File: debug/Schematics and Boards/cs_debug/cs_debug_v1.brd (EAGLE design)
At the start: 38.1 x 44.5 mm, 239 parts, among them J1 J-JTAG-CORTEX_SMD, J19 Solar, J2 J-JTAG-CORTEX_SMD, J3 J-JTAG-CORTEX-NEEDLE6-LEGS, J4 J-SERIAL-PORT, J5 J-WURTH-USBC, Q10 2N7002P, Q3 FDN340P, Q4 2N7002P, Q5 FDN340P, Q6 2N7002P, Q7 FDN340P, Q8 2N7002P, Q9 FDN340P, U1 AP2120N-3.3TRG1, U10 OPA357AIDBVTG4, U11 DAC7574IDGS, U12 MCP73871T-2CCI/ML, U13 USB2412-DZK, U14 INA225AIDGK, U15 OPA357AIDBVTG4, U2 TLV1117LV33DCYR, U5 INA225AIDGK, U6 OPA357AIDBVTG4, U7 INA225AIDGK, U8 OPA357AIDBVTG4, U9 INA225AIDGK, Y1 EPSON_TSX-3225_24.0000MF10Z-C3, Y101 32.768kHz, Y102 12mHz-12pF-K7

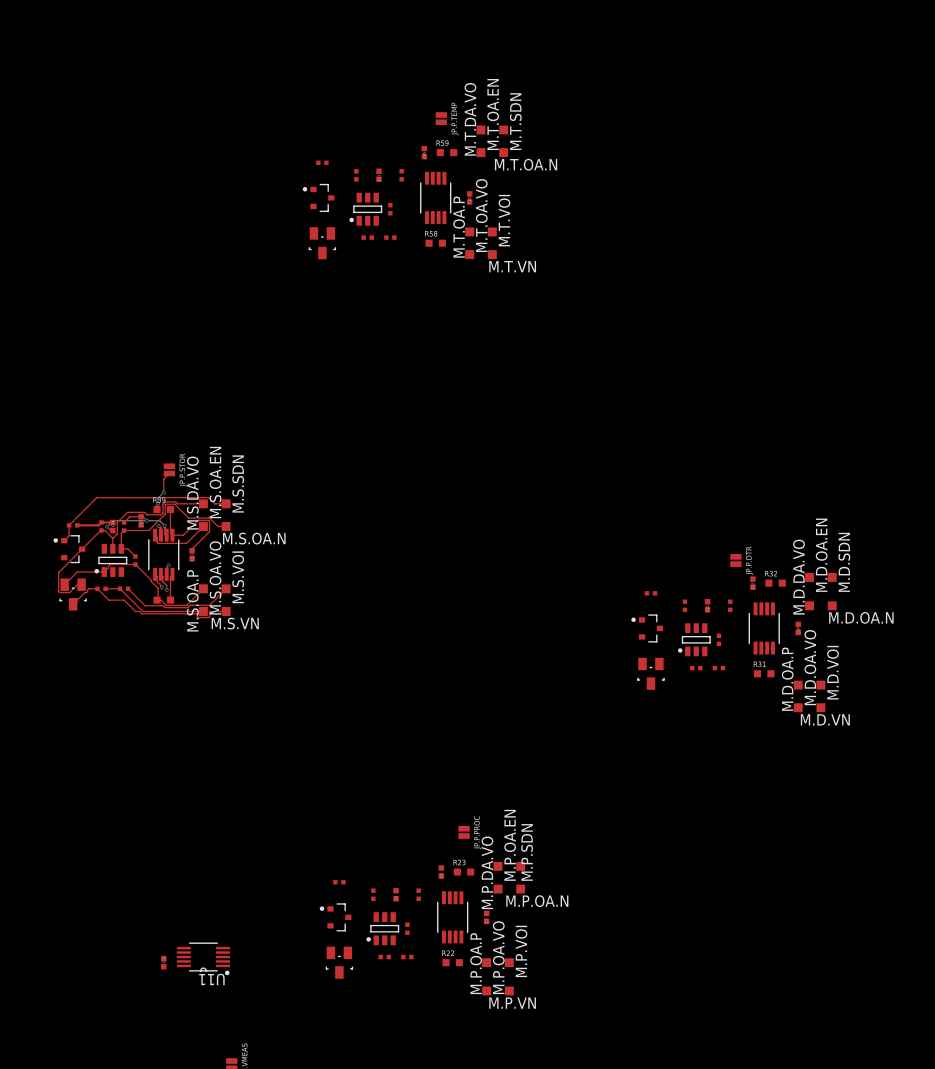
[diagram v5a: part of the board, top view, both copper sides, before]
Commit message: DBG- layout and hand-route for current monitors
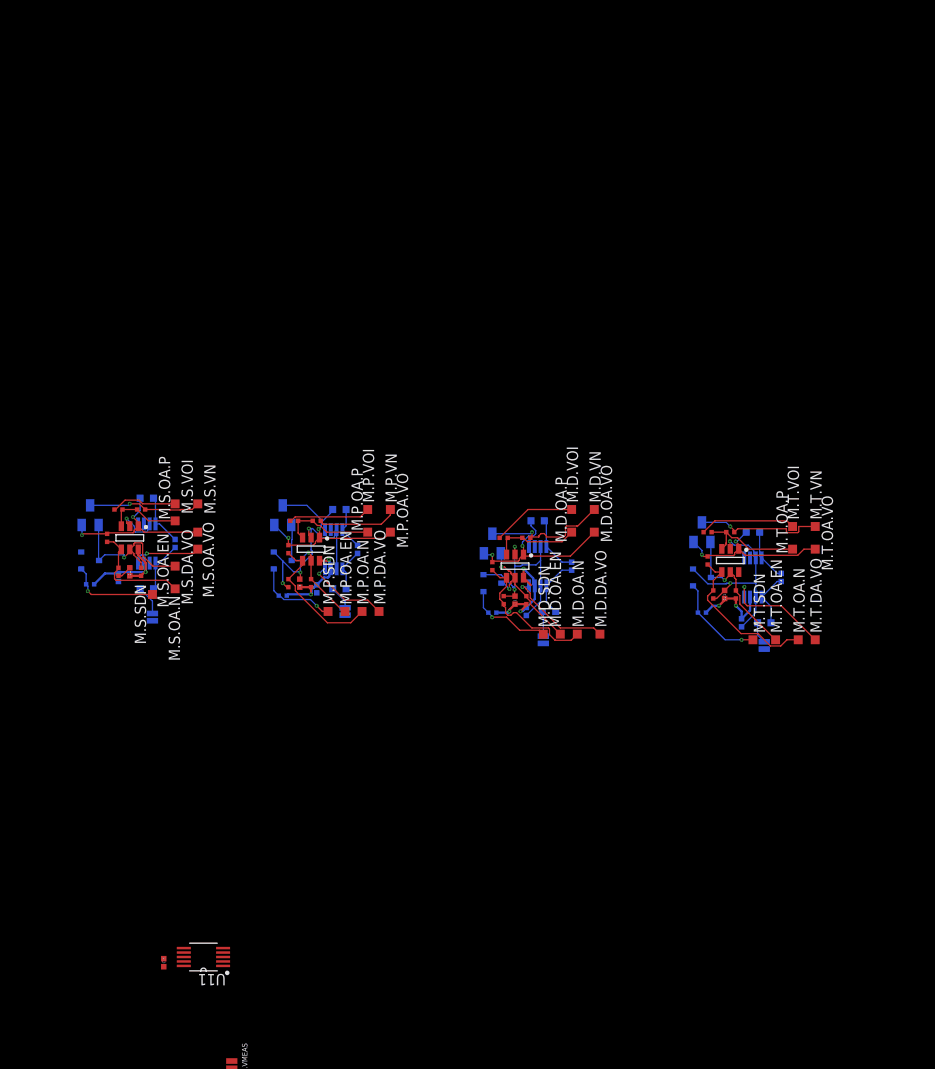
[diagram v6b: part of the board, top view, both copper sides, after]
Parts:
- moved JP.P.TEMP 69.3 mm to (154.9, 17.8), flipped to the bottom, turned to 90 degrees
- moved M.T.DA.VO 66.2 mm to (160.7, 18.4)
- moved M.T.OA.EN 66.0 mm to (156.2, 18.4)
- moved R57 66.0 mm to (148.0, 21.5), flipped to the bottom, turned to 180 degrees
- moved M.T.OA.N 63.8 mm to (158.8, 18.4), turned to 270 degrees
- moved M.T.SDN 63.6 mm to (153.7, 18.4)
- moved C45 63.6 mm to (152.4, 20.3), flipped to the bottom, turned to 270 degrees
- moved R59 63.6 mm to (154.9, 20.3), flipped to the bottom, turned to 180 degrees
- moved R54 63.4 mm to (151.8, 23.5)
- moved C21 60.9 mm to (150.5, 23.5)
- moved Q10 60.2 mm to (148.0, 25.4), flipped to the bottom, turned to 90 degrees
- moved R56 58.5 mm to (149.2, 23.5), turned to 90 degrees
- moved U15 56.6 mm to (151.1, 27.3), turned to 270 degrees
- moved M.P.VN 55.6 mm to (113.0, 33.0), turned to 0 degrees
- moved U14 55.4 mm to (153.7, 25.4), flipped to the bottom, turned to 90 degrees
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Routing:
- net AGND: track 13.0 -> 77.5 mm, vias 4 -> 8
- net 3V3_INSTR_MEAS: track 5.27 -> 46.3 mm, vias 1 -> 8
- net CM_OPAMP_OUT3: track 0.00 -> 20.0 mm, vias 0 -> 2
- net CM_OPAMP_OUT4: track 0.00 -> 19.1 mm, vias 0 -> 2
- net CM_OPAMP_N1: track 0.00 -> 18.3 mm
- net CM_OPAMP_OUT1: track 0.00 -> 18.2 mm, vias 0 -> 2
- net CM_OPAMP_N3: track 0.00 -> 16.7 mm
- net CM_OPAMP_ENABLE1: track 0.00 -> 16.5 mm, vias 0 -> 1
- net CM_OPAMP_N4: track 0.00 -> 15.8 mm
- net CM_OPAMP_ENABLE3: track 0.00 -> 14.8 mm, vias 0 -> 2
- net CM_OPAMP_ENABLE4: track 0.00 -> 14.7 mm, vias 0 -> 1
- net CM_DTR_V_SENSE_N: track 0.00 -> 14.6 mm, vias 0 -> 1
- net CM_TEMP_V_SENSE_N: track 0.00 -> 14.4 mm, vias 0 -> 1
- net CM_PROC_V_SENSE_N: track 0.00 -> 14.0 mm
- net CM_TEMP_DIFFAMP_OUT: track 0.00 -> 12.6 mm, vias 0 -> 1
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
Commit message: DBG-placement on board
It's pretty large; about 3.5x2.5. Lots of ports and test points that need to be accessible.  Test points should probably be moved around so the text is more readable.

Everything important to touch is top-side, and pushed to the exterior of the board.

The boundaries of the board push out to the side such that the physical platform should be pretty stable (in terms of balance w/o a bunch of cables coming off of it.
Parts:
- moved M.T.VN 136.4 mm to (27.3, 59.7), turned to 180 degrees
- moved M.T.OA.VO 134.5 mm to (29.8, 59.7), turned to 0 degrees
- moved M.T.VOI 133.4 mm to (27.3, 57.1), turned to 0 degrees
- moved M.T.OA.P 131.4 mm to (29.8, 57.1), turned to 180 degrees
- moved R58 127.7 mm to (27.9, 52.7), turned to 90 degrees
- moved C20 127.5 mm to (33.0, 55.9), turned to 180 degrees
- moved M.T.DA.VO 127.5 mm to (40.0, 59.7), turned to 180 degrees
- moved M.T.OA.N 125.1 mm to (40.0, 57.8), turned to 0 degrees
- moved R53 124.8 mm to (27.9, 50.2), turned to 270 degrees
- moved U14 123.7 mm to (33.0, 52.7), turned to 0 degrees
- moved U15 122.2 mm to (31.1, 50.2), turned to 0 degrees
- moved M.T.OA.EN 121.9 mm to (40.0, 55.2), turned to 180 degrees
- moved R40 121.9 mm to (27.9, 47.6), turned to 90 degrees
- moved R59 121.6 mm to (38.1, 54.0), turned to 90 degrees
- moved Q9 121.1 mm to (27.9, 47.0), turned to 270 degrees
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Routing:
- net CM_OPAMP_OUT2: track 18.7 -> 26.8 mm
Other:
- board size 38.1 x 44.5 mm -> 83.2 x 62.2 mm

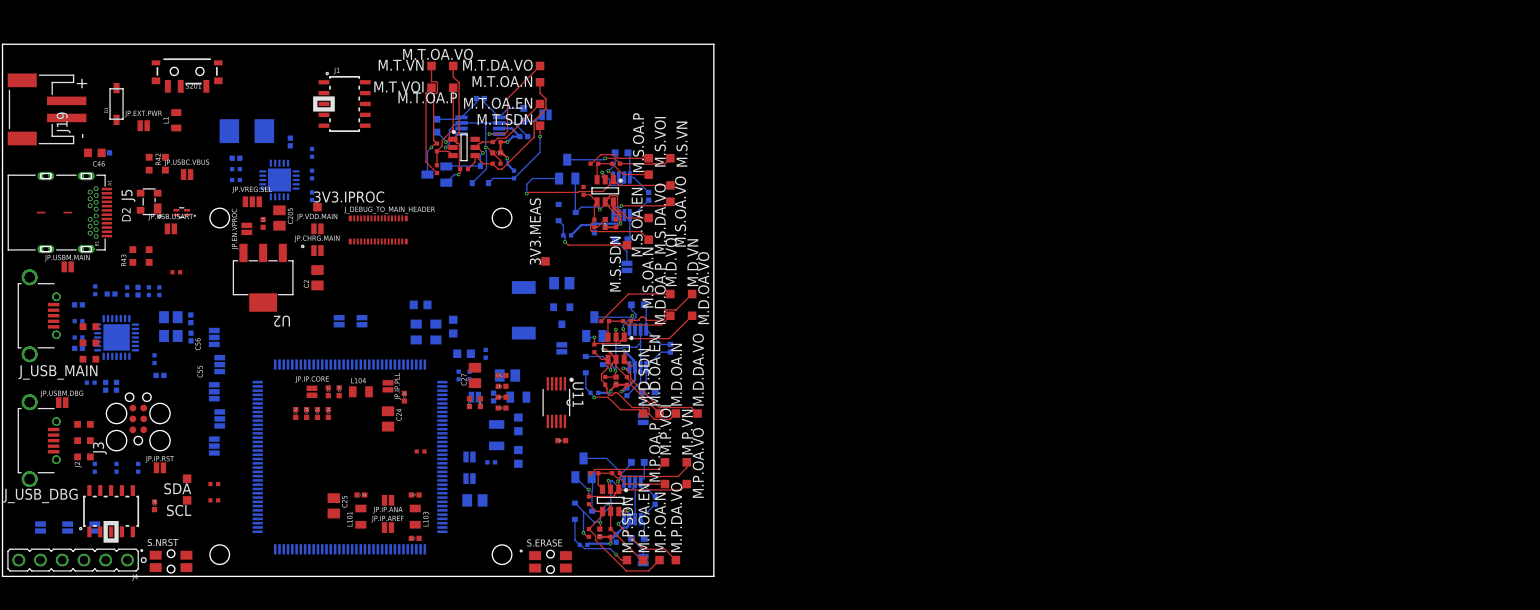
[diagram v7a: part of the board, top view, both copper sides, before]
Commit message: DBG-routing for differential USB signals, update placements
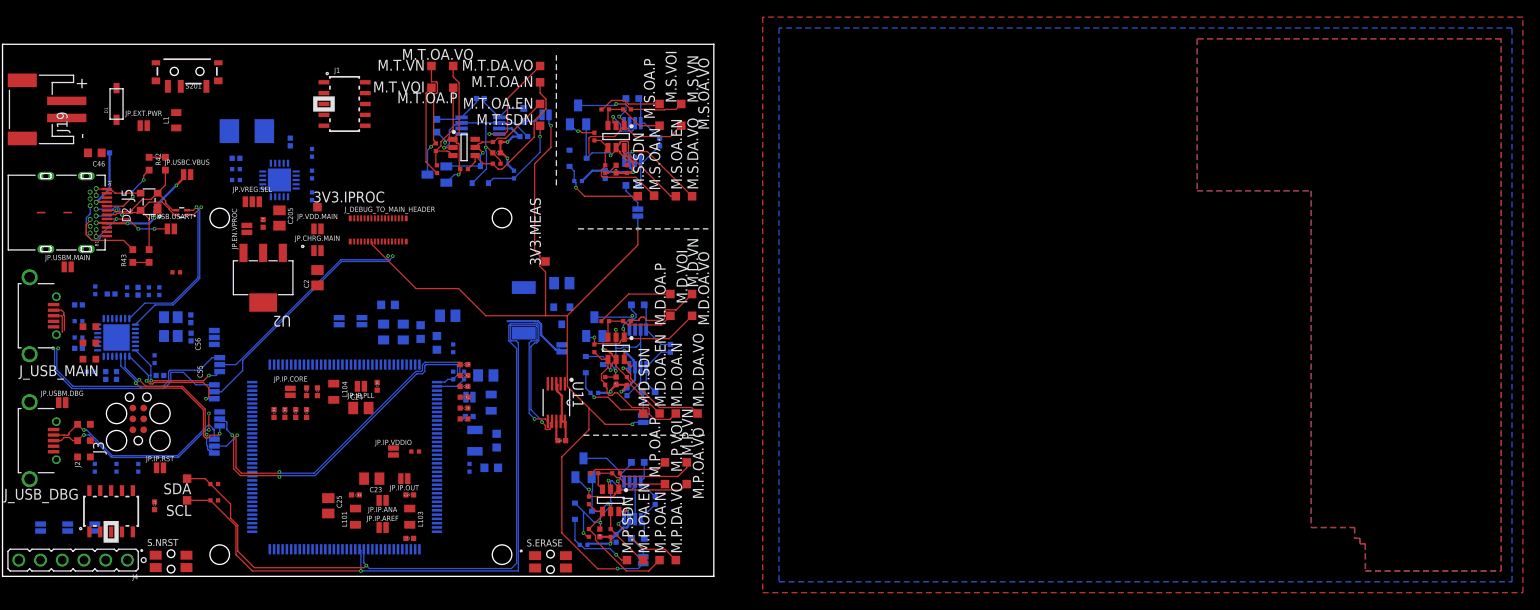
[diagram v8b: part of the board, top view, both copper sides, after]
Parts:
- moved C23 12.3 mm to (20.3, 11.4), flipped to the top
- moved JP.IP.VDDIO 8.91 mm to (22.9, 14.6), flipped to the top, turned to 90 degrees
- moved C27 7.67 mm to (29.2, 30.5), flipped to the bottom, turned to 0 degrees
- moved JP.IP.OUT 7.62 mm to (24.1, 11.4), flipped to the top
- moved M.S.OA.VO 7.10 mm to (56.5, 52.7)
- moved C39 6.75 mm to (31.1, 24.8), turned to 180 degrees
- moved C14 6.48 mm to (48.9, 47.6)
- moved C15 6.48 mm to (47.6, 47.0)
- moved JP.P.STOR 6.48 mm to (51.4, 42.5)
- moved Q5 6.48 mm to (44.5, 54.0)
- moved Q6 6.48 mm to (44.5, 48.9)
- moved R24 6.48 mm to (47.6, 54.6)
- moved R36 6.48 mm to (47.6, 47.6)
- moved R37 6.48 mm to (44.5, 46.2)
- moved U10 6.48 mm to (48.9, 51.4)
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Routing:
- net V_SENSE_P: track 0.00 -> 113.5 mm, vias 0 -> 4
- net INSTR_PROC_I2C_SDA: track 0.00 -> 94.9 mm, vias 0 -> 2
- net INSTR_PROC_I2C_SCL: track 0.00 -> 92.7 mm, vias 0 -> 2
- net INSTR_PROC_USB_D_N: track 0.00 -> 45.2 mm, vias 0 -> 2
- net INSTR_PROC_USB_D_P: track 0.00 -> 43.4 mm, vias 0 -> 2
- net MAIN_USB_DATA_P: track 0.00 -> 28.2 mm, vias 0 -> 1
- net USB_BKUP_MAIN_D_N: track 0.00 -> 27.8 mm, vias 0 -> 1
- net USB_BKUP_MAIN_D_P: track 0.00 -> 27.4 mm, vias 0 -> 1
- net MAIN_USB_DATA_N: track 0.00 -> 25.2 mm, vias 0 -> 1
- net USB_BKUP_DBG_D_N: track 0.00 -> 23.8 mm, vias 0 -> 1
- net USB_BKUP_DBG_D_P: track 0.00 -> 23.1 mm, vias 0 -> 3
- net USBC_VBUS: track 0.00 -> 22.6 mm, vias 0 -> 3
- net USB_D_P: track 0.00 -> 20.2 mm, vias 0 -> 1
- net USB_D_N: track 0.00 -> 19.6 mm, vias 0 -> 1
- net HUB_INSTR_PROC_USB_D_P: track 0.00 -> 19.4 mm, vias 0 -> 2
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- added copper zone on layer 1, net AGND
- added copper zone on layer 16, net AGND1
- added copper zone on layer 1, net DGND
- added copper zone on layer 16, net DGND
